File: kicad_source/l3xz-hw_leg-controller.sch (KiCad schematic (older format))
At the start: 8 parts, among them CN1 ARDUINO_NANO_33

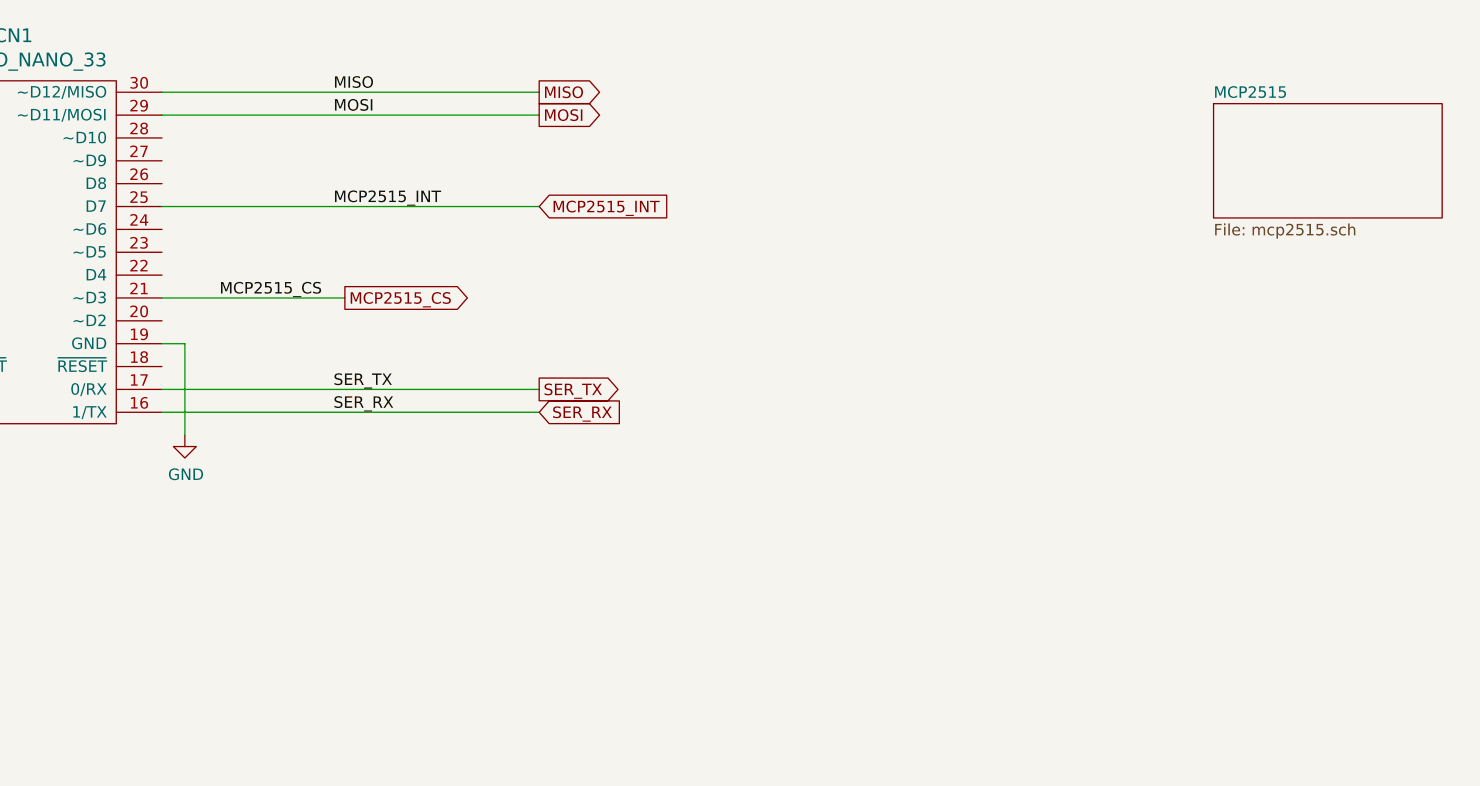
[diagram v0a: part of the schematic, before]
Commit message: added rotary encoder, led and switch
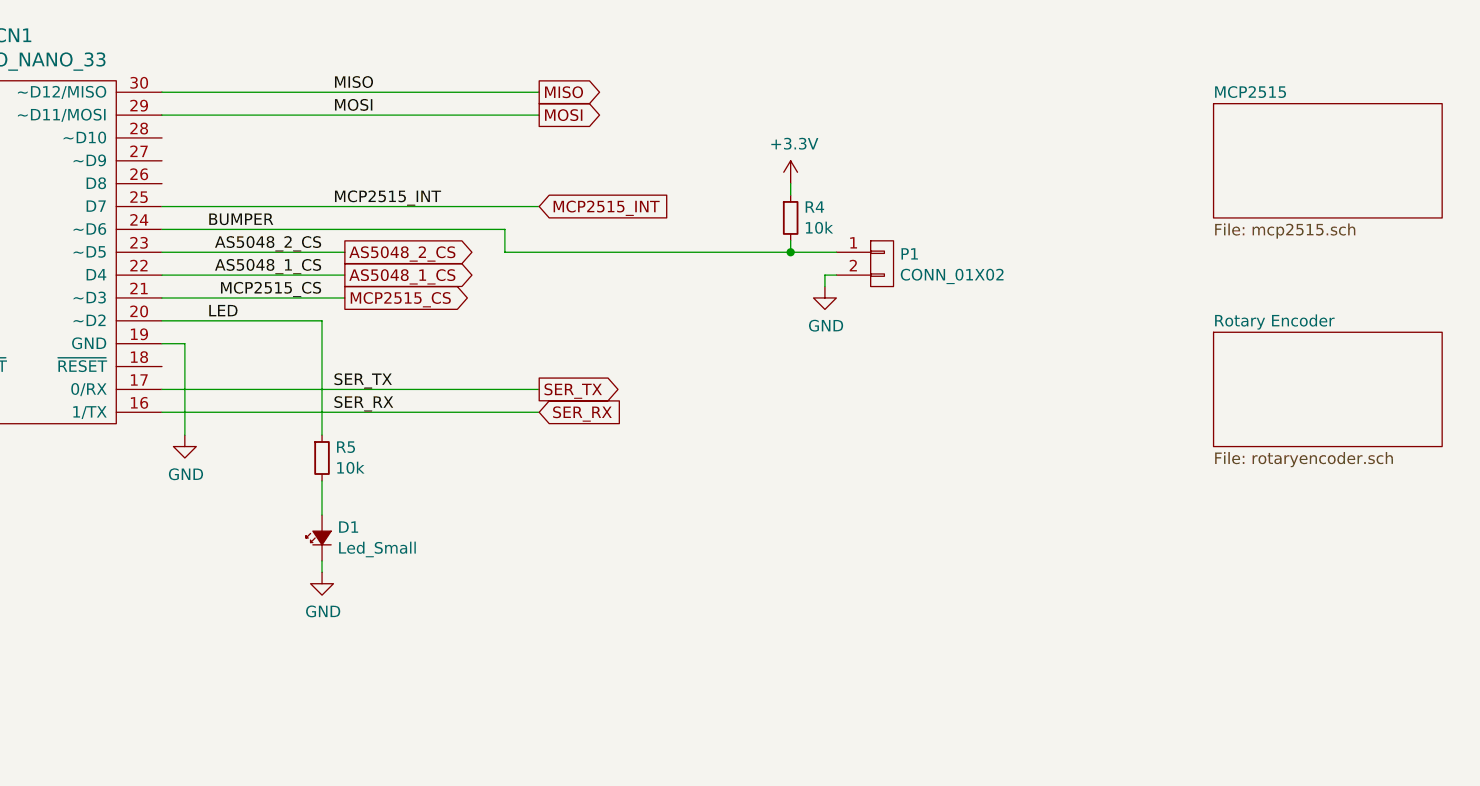
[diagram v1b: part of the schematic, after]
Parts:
- added D1: Led_Small, LEDs:LED_0603, symbol devices:Led_Small
- added P1: CONN_01X02, CON_wuerth:WR-TBL_691382000002, symbol mechanical-connectors:CONN_01X02
- added R4, R5: 10k, resistors:R_0603, symbol devices:R_0603
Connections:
- net +3V3: now also R4.1
- net GND: now also D1.1 (K), P1.2 (P2)
- net LED: now reaches CN1.20 (~~D2)
- net LED: now also R5.1
- net AS5048_1_CS: now reaches CN1.22 (D4)
- net AS5048_2_CS: now reaches CN1.23 (~~D5)
- net BUMPER: now reaches CN1.24 (~~D6)
- net BUMPER: now also P1.1 (P1), R4.2
- new net: D1.2 (A), R5.2
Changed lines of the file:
@@
 $Descr A4 11693 8268
 encoding utf-8
-Sheet 1 2
+Sheet 1 3
 Title "l3xz-hw_leg-controller"
 Date "2022-04-03"
@@
 Wire Wire Line
 	3500 3750 3500 3950
+$Sheet
+S 9500 3500 1000 500
+U 624A3AB1
+F0 "Rotary Encoder" 50
+F1 "rotaryencoder.sch" 50
+$EndSheet
+Wire Wire Line
+	5700 3250 4900 3250
+Text Label 5600 3250 2    50   ~ 0
+AS5048_1_CS
+Text GLabel 5700 3250 2    50   Output ~ 0
+AS5048_1_CS
+Wire Wire Line
+	5700 3150 4900 3150
+Text Label 5600 3150 2    50   ~ 0
+AS5048_2_CS
+Text GLabel 5700 3150 2    50   Output ~ 0
+AS5048_2_CS
+$Comp
+L devices:Led_Small D1
+U 1 1 624BD2BD
+P 5600 4400
+F 0 "D1" V 5646 4332 50  0000 R CNN
+F 1 "Led_Small" V 5555 4332 50  0000 R CNN
+F 2 "LEDs:LED_0603" V 5600 4400 50  0001 C CNN
+F 3 "" V 5600 4400 50  0000 C CNN
+	1    5600 4400
+	0    -1   -1   0
+$EndComp
+$Comp
+L devices:R_0603 R?
+U 1 1 624BFD41
+P 5600 4050
+AR Path="/5ED92F9C/624BFD41" Ref="R?"  Part="1"
+AR Path="/624BFD41" Ref="R5"  Part="1"
+F 0 "R5" H 5659 4096 50  0000 L CNN
+F 1 "10k" H 5659 4005 50  0000 L CNN
+F 2 "resistors:R_0603" H 5600 3900 50  0001 C CNN
+F 3 "" H 5600 4050 50  0000 C CNN
+	1    5600 4050
+	1    0    0    -1
+$EndComp
+$Comp
+L power-supply:+3.3V #PWR?
+U 1 1 624BFD47
+P 7650 2850
+AR Path="/5ED92F9C/624BFD47" Ref="#PWR?"  Part="1"
+AR Path="/624BFD47" Ref="#PWR03"  Part="1"
+F 0 "#PWR03" H 7650 2700 50  0001 C CNN
+F 1 "+3.3V" H 7665 3023 50  0000 C CNN
+F 2 "" H 7650 2850 50  0000 C CNN
+F 3 "" H 7650 2850 50  0000 C CNN
+	1    7650 2850
+	1    0    0    -1
+$EndComp
+$Comp
+L power-supply:GND #PWR05
+U 1 1 624C1143
+P 5600 4550
+F 0 "#PWR05" H 5600 4300 50  0001 C CNN
+F 1 "GND" H 5605 4377 50  0000 C CNN
+F 2 "" H 5600 4550 50  0000 C CNN
+F 3 "" H 5600 4550 50  0000 C CNN
+	1    5600 4550
+	1    0    0    -1
+$EndComp
+Wire Wire Line
+	4900 3450 5600 3450
+Wire Wire Line
+	5600 3450 5600 3950
+Wire Wire Line
+	5600 4150 5600 4300
+Wire Wire Line
+	5600 4500 5600 4550
+$Comp
+L mechanical-connectors:CONN_01X02 P1
+U 1 1 624C3078
+P 8050 3200
+F 0 "P1" H 8128 3241 50  0000 L CNN
+F 1 "CONN_01X02" H 8128 3150 50  0000 L CNN
+F 2 "CON_wuerth:WR-TBL_691382000002" H 8128 3104 50  0001 L CNN
+F 3 "" H 8050 3200 50  0000 C CNN
+	1    8050 3200
+	1    0    0    -1
+$EndComp
+$Comp
+L devices:R_0603 R?
+U 1 1 624C3C6E
+P 7650 3000
+AR Path="/5ED92F9C/624C3C6E" Ref="R?"  Part="1"
+AR Path="/624C3C6E" Ref="R4"  Part="1"
+F 0 "R4" H 7709 3046 50  0000 L CNN
+F 1 "10k" H 7709 2955 50  0000 L CNN
+F 2 "resistors:R_0603" H 7650 2850 50  0001 C CNN
+F 3 "" H 7650 3000 50  0000 C CNN
+	1    7650 3000
+	1    0    0    -1
+$EndComp
+$Comp
+L power-supply:GND #PWR04
+U 1 1 624C581E
+P 7800 3300
+F 0 "#PWR04" H 7800 3050 50  0001 C CNN
+F 1 "GND" H 7805 3127 50  0000 C CNN
+F 2 "" H 7800 3300 50  0000 C CNN
+F 3 "" H 7800 3300 50  0000 C CNN
+	1    7800 3300
+	1    0    0    -1
+$EndComp
+Wire Wire Line
+	7850 3150 7650 3150
+Wire Wire Line
+	6400 3150 6400 3050
+Wire Wire Line
+	6400 3050 4900 3050
+Wire Wire Line
+	7650 2900 7650 2850
+Wire Wire Line
+	7650 3100 7650 3150
+Connection ~ 7650 3150
+Wire Wire Line
+	7650 3150 6400 3150
+Wire Wire Line
+	7800 3250 7800 3300
+Wire Wire Line
+	7850 3250 7800 3250
+Text Label 5100 3450 0    50   ~ 0
+LED
+Text Label 5100 3050 0    50   ~ 0
+BUMPER
 $EndSCHEMATC

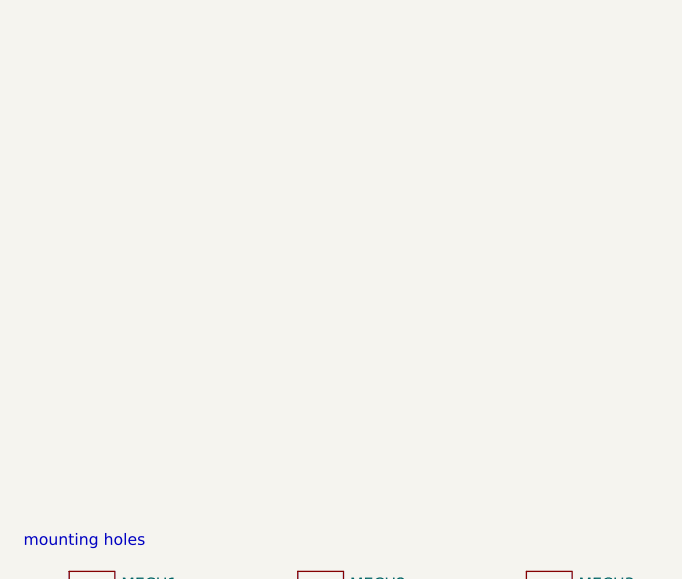
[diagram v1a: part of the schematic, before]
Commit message: added dronecode can and qwiic connectors
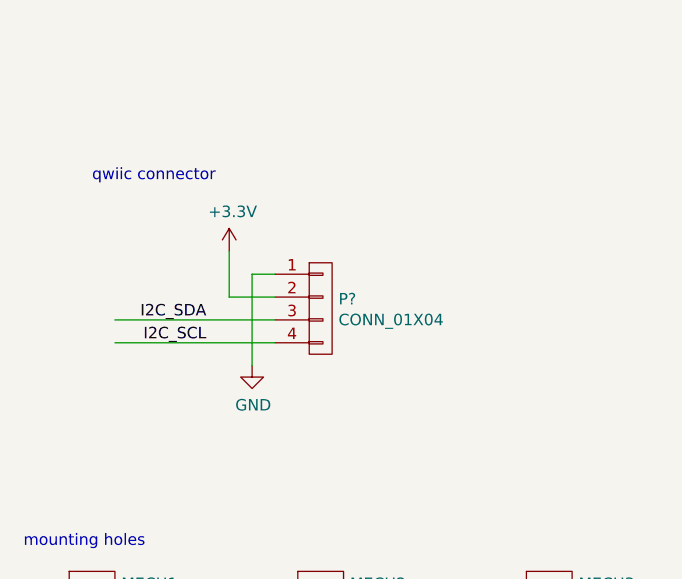
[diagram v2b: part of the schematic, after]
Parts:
- added P?: CONN_01X04, symbol mechanical-connectors:CONN_01X04
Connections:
- wire segments 29 -> 35
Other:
- note added: "qwiic connector"
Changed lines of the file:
@@
 Text Label 5100 3050 0    50   ~ 0
 BUMPER
+$Comp
+L mechanical-connectors:CONN_01X04 P?
+U 1 1 6250C797
+P 2000 6350
+F 0 "P?" H 2078 6391 50  0000 L CNN
+F 1 "CONN_01X04" H 2078 6300 50  0000 L CNN
+F 2 "" H 2000 6350 50  0000 C CNN
+F 3 "" H 2000 6350 50  0000 C CNN
+	1    2000 6350
+	1    0    0    -1
+$EndComp
+$Comp
+L power-supply:GND #PWR?
+U 1 1 6250D556
+P 1700 6600
+F 0 "#PWR?" H 1700 6350 50  0001 C CNN
+F 1 "GND" H 1705 6427 50  0000 C CNN
+F 2 "" H 1700 6600 50  0000 C CNN
+F 3 "" H 1700 6600 50  0000 C CNN
+	1    1700 6600
+	1    0    0    -1
+$EndComp
+$Comp
+L power-supply:+3.3V #PWR?
+U 1 1 6250E35F
+P 1600 6100
+AR Path="/5ED92F9C/6250E35F" Ref="#PWR?"  Part="1"
+AR Path="/6250E35F" Ref="#PWR?"  Part="1"
+F 0 "#PWR?" H 1600 5950 50  0001 C CNN
+F 1 "+3.3V" H 1615 6273 50  0000 C CNN
+F 2 "" H 1600 6100 50  0000 C CNN
+F 3 "" H 1600 6100 50  0000 C CNN
+	1    1600 6100
+	1    0    0    -1
+$EndComp
+Wire Wire Line
+	1800 6300 1600 6300
+Wire Wire Line
+	1600 6300 1600 6100
+Wire Wire Line
+	1800 6200 1700 6200
+Wire Wire Line
+	1700 6200 1700 6600
+Wire Wire Line
+	1100 6400 1800 6400
+Wire Wire Line
+	1100 6500 1800 6500
+Text Label 1500 6400 2    50   ~ 0
+I2C_SDA
+Text Label 1500 6500 2    50   ~ 0
+I2C_SCL
+Text Notes 1000 5800 0    50   ~ 0
+qwiic connector
 $EndSCHEMATC

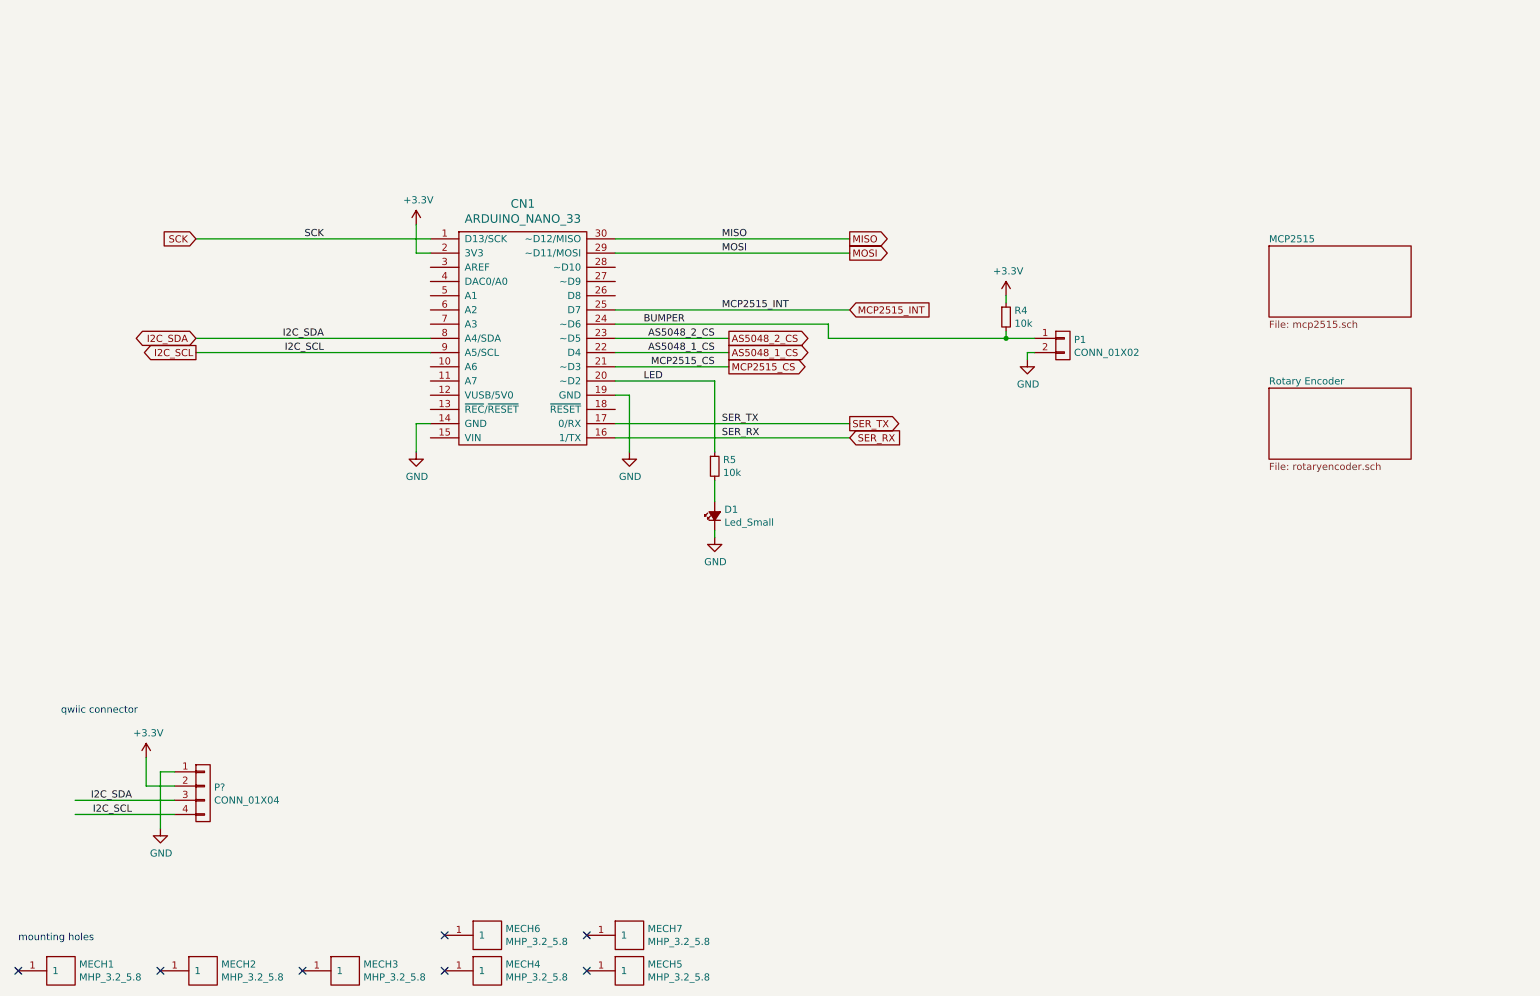
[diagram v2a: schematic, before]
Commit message: added eeprom and servo connectors, updated pdf
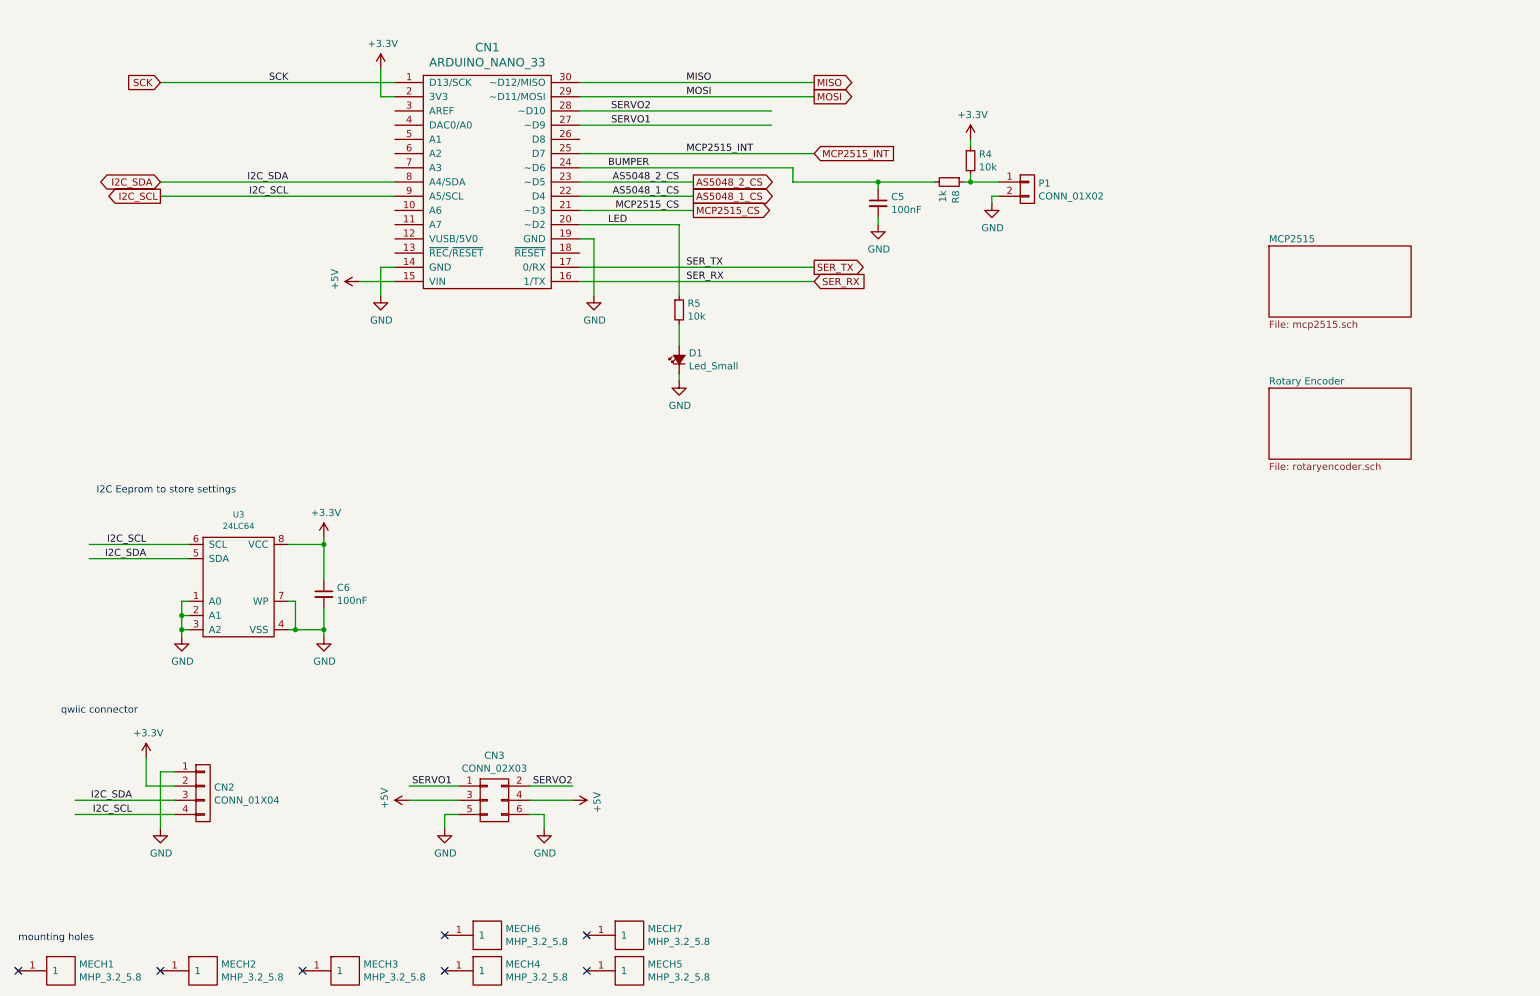
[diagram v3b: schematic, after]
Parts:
- added C5, C6: 100nF, capacitors:C_0603, symbol devices:C_0603
- added CN3: CONN_02X03, symbol mechanical-connectors:CONN_02X03
- added R8: 1k, resistors:R_0603, symbol devices:R_0603
- added U3: 24LC64, SOIC:SOIC-8_3.9x4.9mm_Pitch1.27mm, symbol IC_interface_i2c:24LC64
- gave numbers to parts that had none: 1
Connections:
- net labels added: +5V, SERVO1, SERVO2
- wire segments 35 -> 67
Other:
- note added: "I2C Eeprom to store settings"
- moved on the sheet: CN1, D1, P1, R4, R5
